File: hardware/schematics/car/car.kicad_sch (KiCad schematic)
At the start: 20 parts, among them M1 Motor_Servo, Q1 PMOS, SW2 SW_Push, SW3 SW_Push, U1 VL53L0CXV0DH1, U10 Mini-560, U11 JGA25-37x, U2 VL53L0CXV0DH1, U3 VL53L0CXV0DH1, U4 Pixy2, U5 TXS0108EPW, U6 TB6612FNG, U7 SparkFun OTOS, U8 SWD debug probe, U9 Mini-360

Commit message: [Schematic] schematic: use TB6612FNG breakout footprint
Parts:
- U6: footprint Package_SO:SSOP-24_5.3x8.2mm_P0.65mm -> xlnc-foot:TB6612FNG_Breakout_Sparkfun
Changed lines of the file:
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@@
 			)
 		)
-		(property "Footprint" "Package_SO:SSOP-24_5.3x8.2mm_P0.65mm"
+		(property "Footprint" "xlnc-foot:TB6612FNG_Breakout_Sparkfun"
 			(at 44.45 186.69 0)
 			(hide yes)

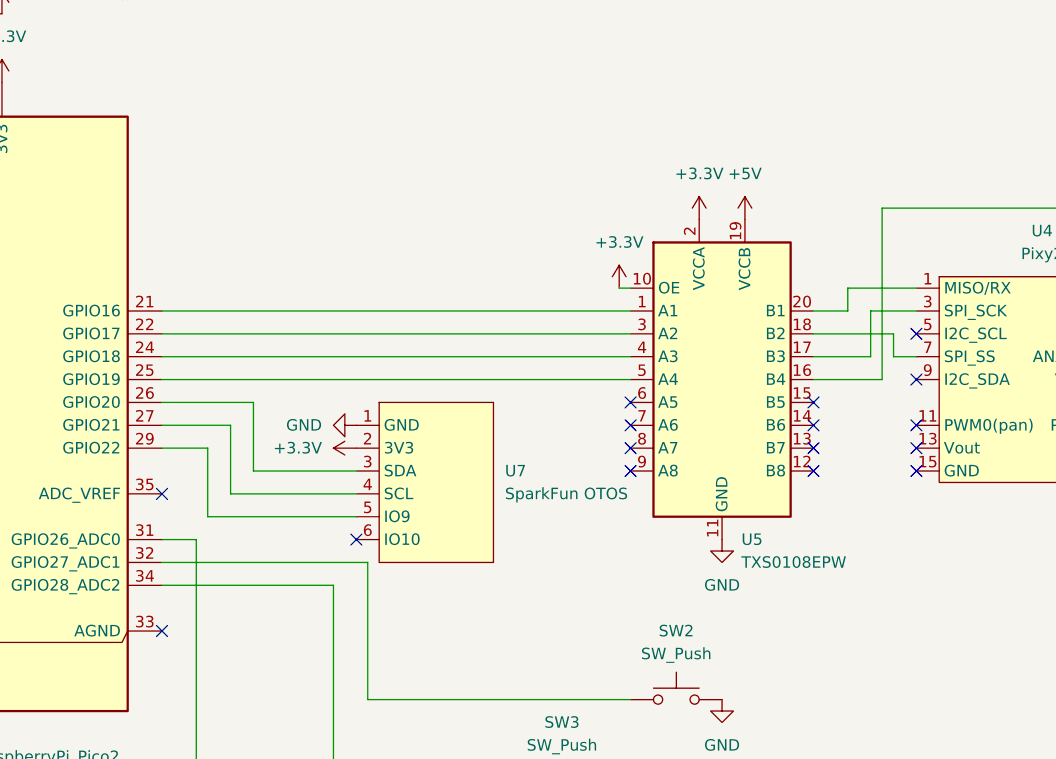
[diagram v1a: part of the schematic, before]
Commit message: [Schematic] Use simpler, smaller level shifter
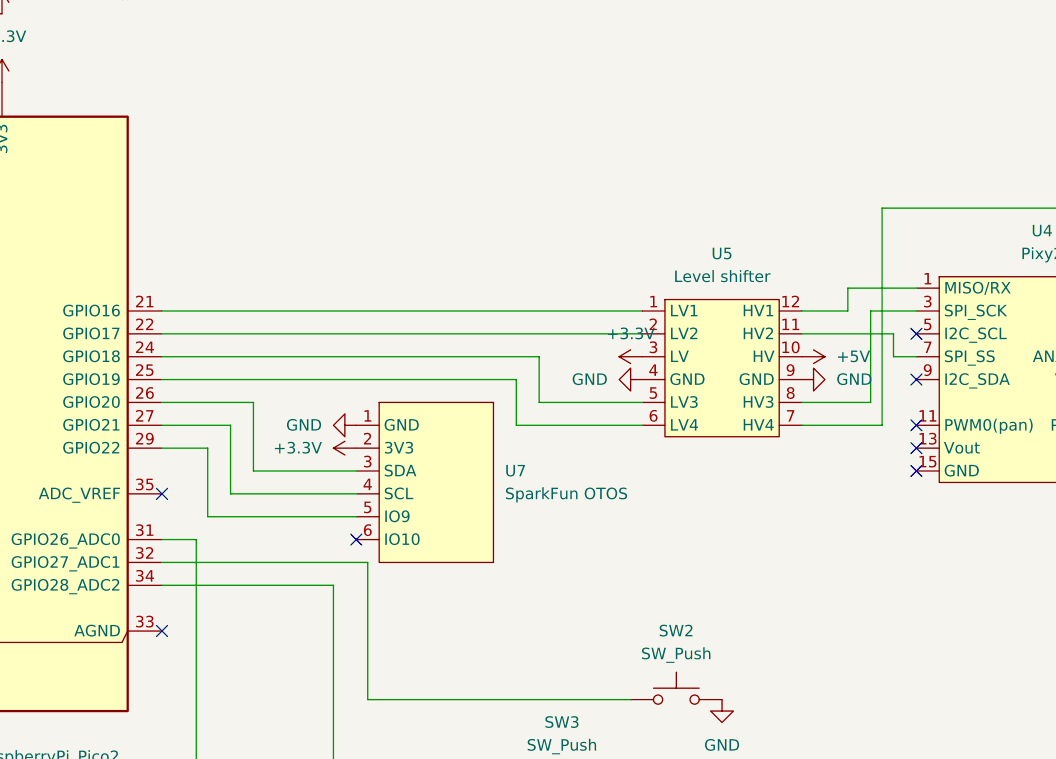
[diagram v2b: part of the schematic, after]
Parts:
- removed U5: TXS0108EPW, Package_SO:TSSOP-20_4.4x6.5mm_P0.65mm, symbol Logic_LevelTranslator:TXS0108EPW
- added U5: Level shifter, xlnc-foot:LevelShifter_4channel_bidirectional, symbol xlnc_apex:LevelShifter_4channel_bidirectional
- BZ1: footprint (none) -> Buzzer_Beeper:Buzzer_TDK_PS1240P02BT_D12.2mm_H6.5mm
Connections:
- net +3.3V: now also U5.3 (LV)
- net +5V: now also U5.10 (HV)
- net GND: now also U5.4 (GND), U5.9 (GND)
- net at A1.21 (GPIO16): now also U5.1 (LV1)
- net at U4.4 (MOSI/TX): now also U5.7 (HV4)
- net at U4.3 (SPI_SCK): now also U5.8 (HV3)
- net at U4.7 (SPI_SS): now also U5.11 (HV2)
- net at U4.1 (MISO/RX): now also U5.12 (HV1)
- net at A1.22 (GPIO17): now also U5.2 (LV2)
- net at A1.24 (GPIO18): now also U5.5 (LV3)
- net at A1.25 (GPIO19): now also U5.6 (LV4)
- no-connect marks 28 -> 20

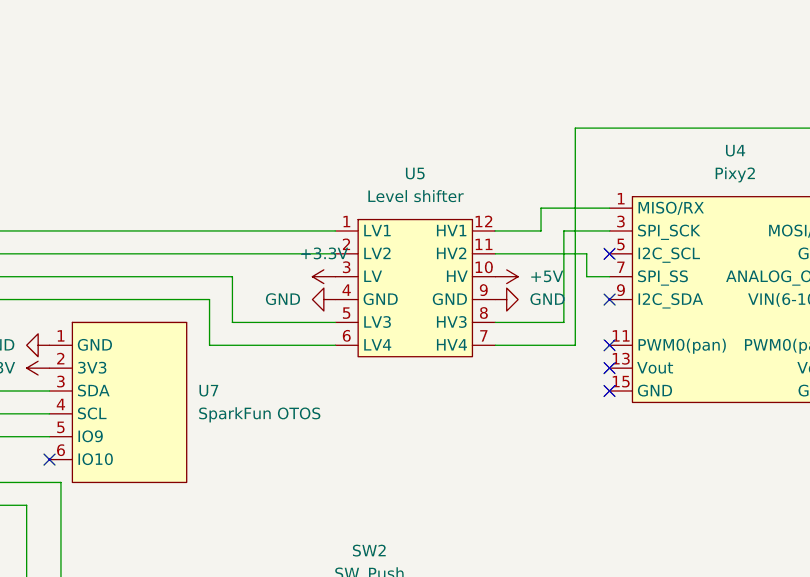
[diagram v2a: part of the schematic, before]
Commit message: [Schematic] Fix super suboptimal connection for level shifter(was like cross thing)
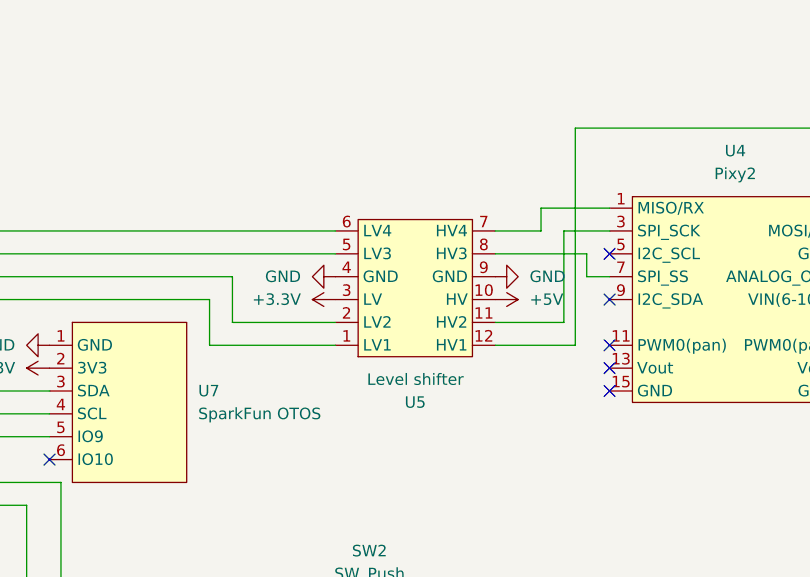
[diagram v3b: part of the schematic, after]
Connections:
- net at U5.1 (LV1): now also A1.25 (GPIO19); no longer A1.21 (GPIO16)
- net at U5.11 (HV2): now also U4.3 (SPI_SCK); no longer U4.7 (SPI_SS)
- net at U5.12 (HV1): now also U4.4 (MOSI/TX); no longer U4.1 (MISO/RX)
- net at U5.2 (LV2): now also A1.24 (GPIO18); no longer A1.22 (GPIO17)
- net at U5.5 (LV3): now also A1.22 (GPIO17); no longer A1.24 (GPIO18)
- net at U5.6 (LV4): now also A1.21 (GPIO16); no longer A1.25 (GPIO19)
- net at U5.7 (HV4): now also U4.1 (MISO/RX); no longer U4.4 (MOSI/TX)
- net at U5.8 (HV3): now also U4.7 (SPI_SS); no longer U4.3 (SPI_SCK)

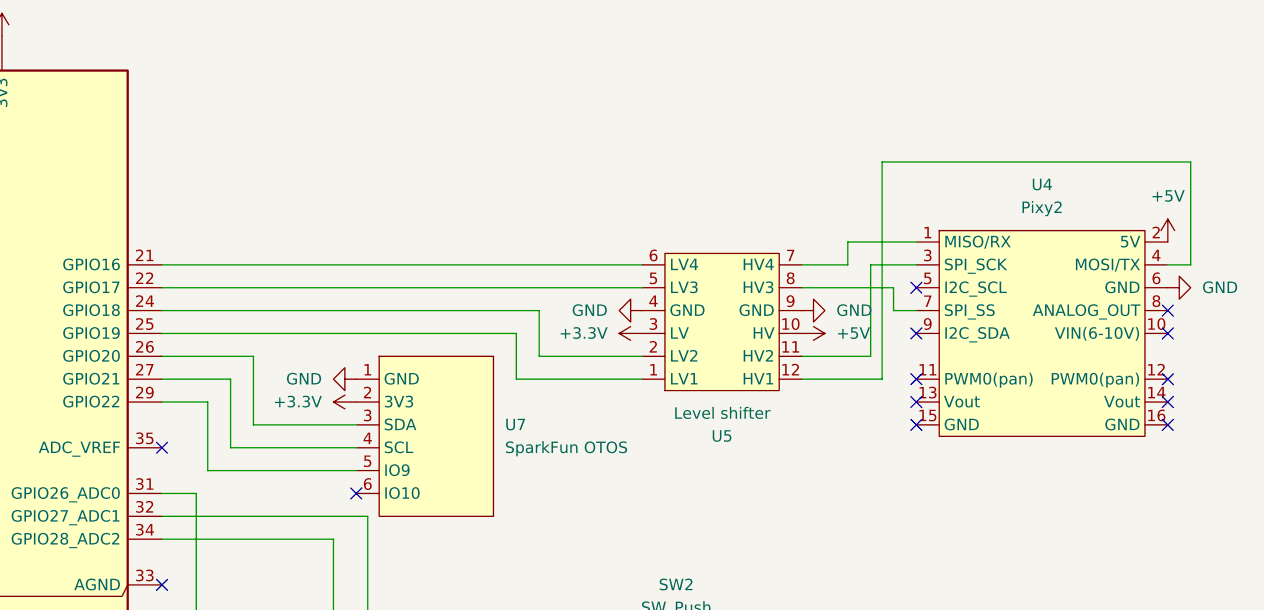
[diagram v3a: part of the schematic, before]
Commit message: [Schematic] Remove level shifter. The pixy2 seems to have 3.3v outputs, maybe 3.3v tolerable input? Need testing.
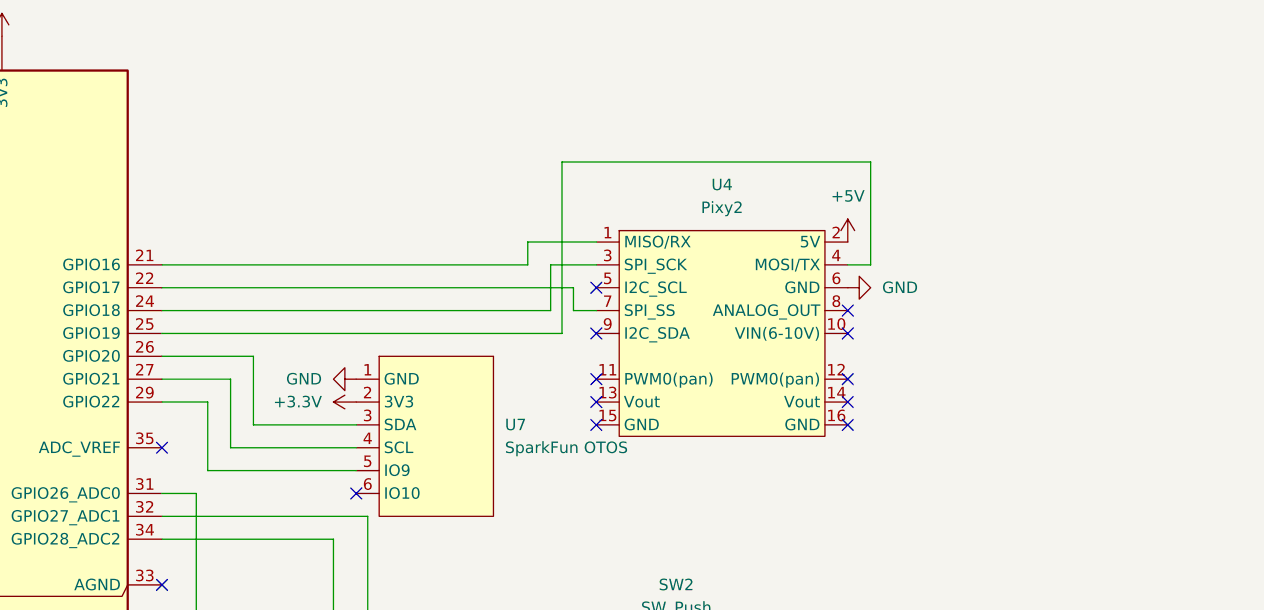
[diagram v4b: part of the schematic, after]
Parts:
- removed U5: Level shifter, xlnc-foot:LevelShifter_4channel_bidirectional, symbol xlnc_apex:LevelShifter_4channel_bidirectional
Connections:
- net at A1.25 (GPIO19): now also U4.4 (MOSI/TX)
- net at U4.3 (SPI_SCK): now also A1.24 (GPIO18)
- net at A1.22 (GPIO17): now also U4.7 (SPI_SS)
- net at A1.21 (GPIO16): now also U4.1 (MISO/RX)
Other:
- moved on the sheet: U4

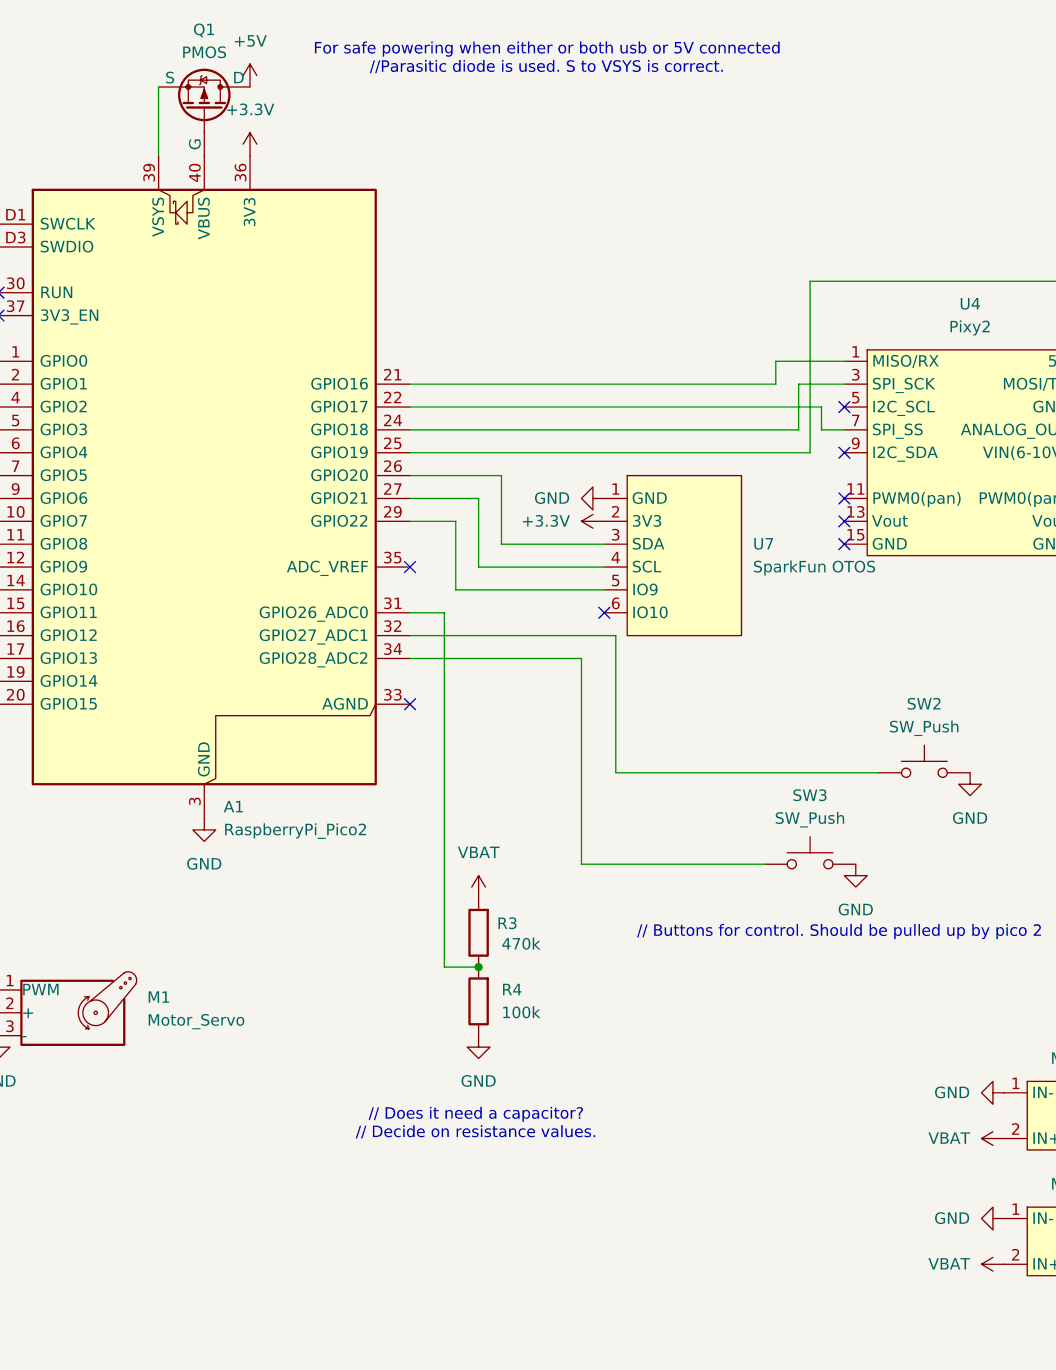
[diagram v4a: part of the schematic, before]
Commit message: [Schematic] fix mosfet, add xt60
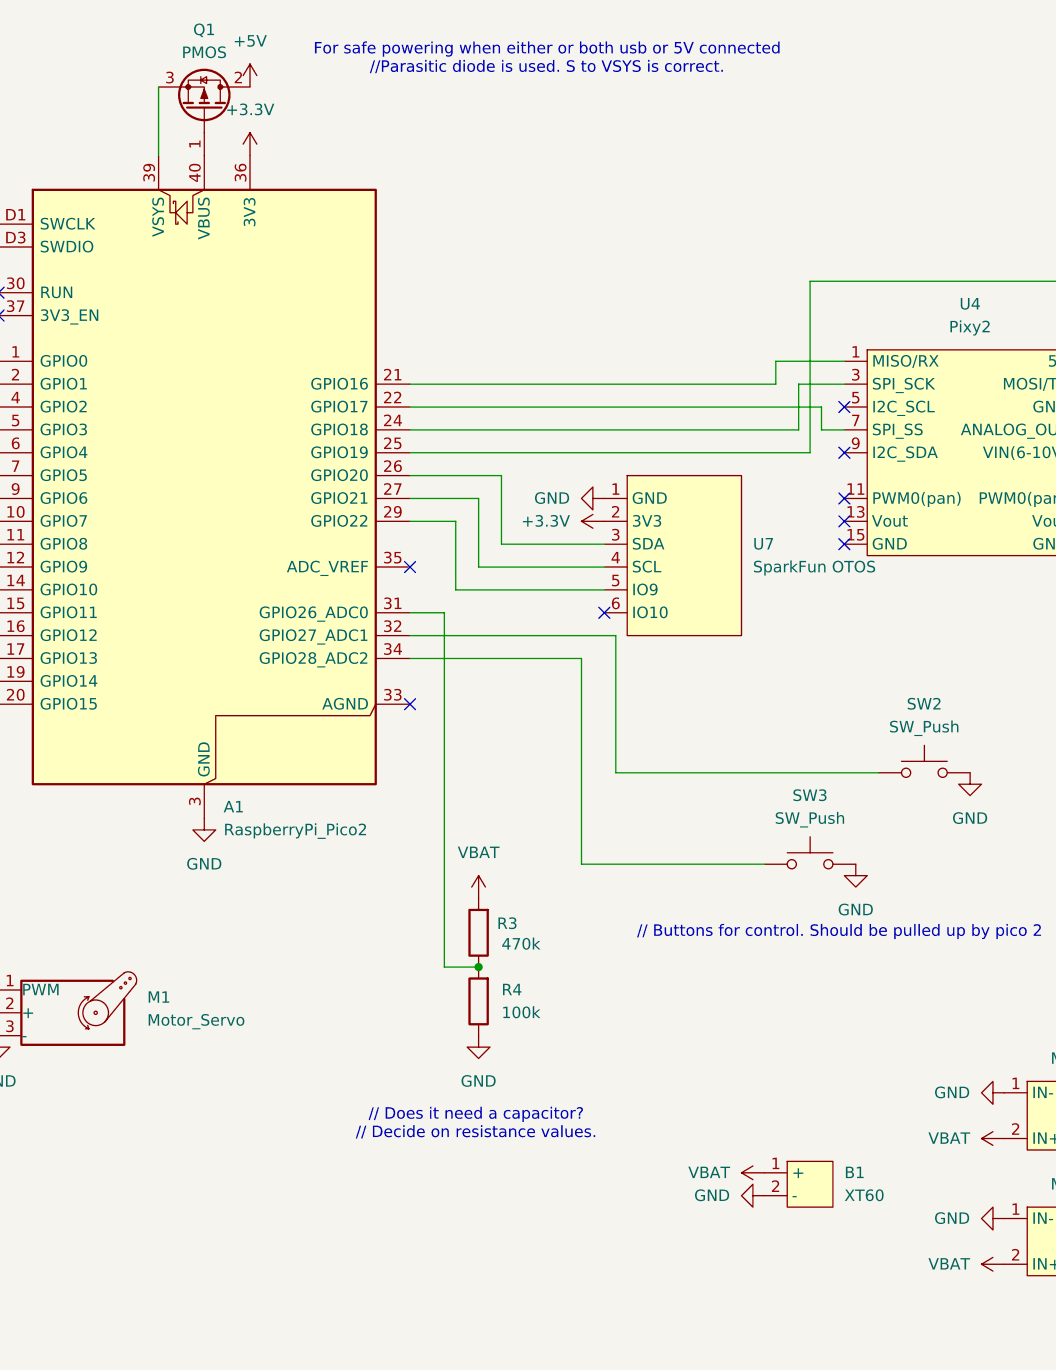
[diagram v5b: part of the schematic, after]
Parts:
- added B1: XT60, xlnc-foot:XT60, symbol xlnc_apex:xt60
- A1: footprint Module:RaspberryPi_Pico_SMD_HandSolder -> Module:RaspberryPi_Pico_Common_THT
- Q1: footprint Package_TO_SOT_THT:TO-247-3_Vertical -> Package_TO_SOT_THT:TO-220F-3_Vertical; symbol Simulation_SPICE:PMOS -> Transistor_FET:Q_PMOS_GDS
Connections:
- net +5V: now also Q1.2 (D); no longer Q1.1 (D)
- net GND: now also B1.2 (-)
- net VBAT: now also B1.1 (+)
- net at A1.40 (VBUS): now also Q1.1 (G); no longer Q1.2 (G)

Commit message: [Schematic] Change button footprint. PCB: move around, connect easy things.
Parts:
- SW2, SW3: footprint Connector_PinHeader_2.54mm:PinHeader_1x02_P2.54mm_Vertical -> xlnc-foot:SW_PUSH_6mm_5.08mm
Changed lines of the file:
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@@
 			)
 		)
-		(property "Footprint" "Connector_PinHeader_2.54mm:PinHeader_1x02_P2.54mm_Vertical"
+		(property "Footprint" "xlnc-foot:SW_PUSH_6mm_5.08mm"
 			(at 208.28 102.87 0)
 			(hide yes)
@@
 			)
 		)
-		(property "Footprint" "Connector_PinHeader_2.54mm:PinHeader_1x02_P2.54mm_Vertical"
+		(property "Footprint" "xlnc-foot:SW_PUSH_6mm_5.08mm"
 			(at 220.98 92.71 0)
 			(hide yes)

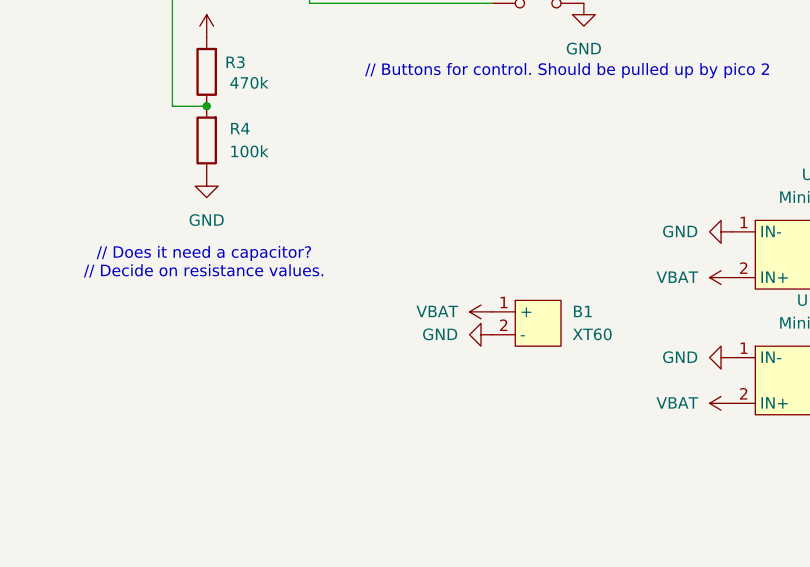
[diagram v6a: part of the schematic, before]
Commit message: [Schematic] Add battery switch.
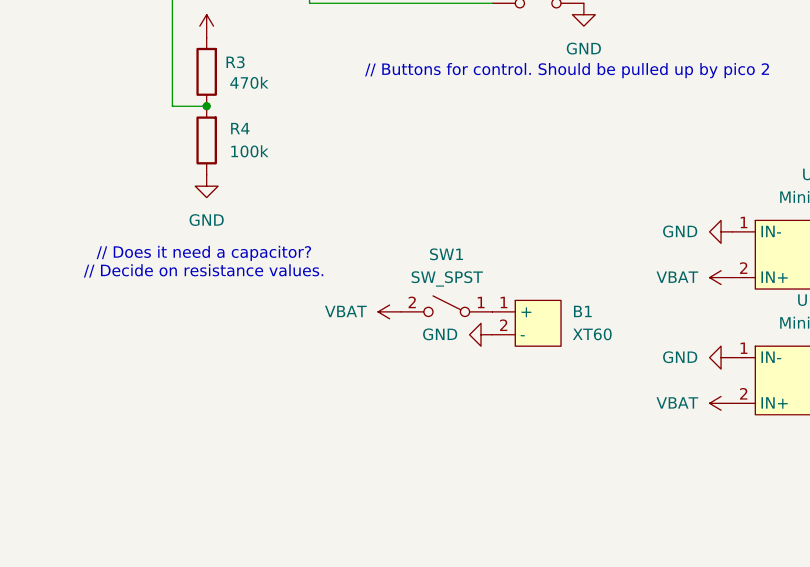
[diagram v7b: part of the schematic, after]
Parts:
- added SW1: SW_SPST, xlnc-foot:SW_SPST_20.96mmx14.74mm, symbol Switch:SW_SPST
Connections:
- net VBAT: now also SW1.2 (B); no longer B1.1 (+)
- new net: B1.1 (+), SW1.1 (A)
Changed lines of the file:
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@@
 	)
 	(symbol
+		(lib_id "Switch:SW_SPST")
+		(at 198.12 142.24 0)
+		(mirror y)
+		(unit 1)
+		(body_style 1)
+		(exclude_from_sim no)
+		(in_bom yes)
+		(on_board yes)
+		(in_pos_files yes)
+		(dnp no)
+		(property "Reference" "SW1"
+			(at 198.12 135.89 0)
+			(show_name no)
+			(do_not_autoplace no)
+			(effects
+				(font
+					(size 1.27 1.27)
+				)
+			)
+		)
+		(property "Value" "SW_SPST"
+			(at 198.12 138.43 0)
+			(show_name no)
+			(do_not_autoplace no)
+			(effects
+				(font
+					(size 1.27 1.27)
+				)
+			)
+		)
+		(property "Footprint" "xlnc-foot:SW_SPST_20.96mmx14.74mm"
+			(at 198.12 142.24 0)
+			(hide yes)
+			(show_name no)
+			(do_not_autoplace no)
+			(effects
+				(font
+					(size 1.27 1.27)
+				)
+			)
+		)
+		(property "Datasheet" ""
+			(at 198.12 142.24 0)
+			(hide yes)
+			(show_name no)
+			(do_not_autoplace no)
+			(effects
+				(font
+					(size 1.27 1.27)
+				)
+			)
+		)
+		(property "Description" "Single Pole Single Throw (SPST) switch"
+			(at 198.12 142.24 0)
+			(hide yes)
+			(show_name no)
+			(do_not_autoplace no)
+			(effects
+				(font
+					(size 1.27 1.27)
+				)
+			)
+		)
+		(pin "1"
+		)
+		(pin "2"
+		)
+		(instances
+			(project "car"
+				(path "/5e1ba60a-5dff-4ce7-a8b0-cf19f27fe16e"
+					(reference "SW1")
+					(unit 1)
+				)
+			)
+		)
+	)
+	(symbol
 		(lib_id "power:GND")
 		(at 247.65 133.35 90)
@@
 	(symbol
 		(lib_id "power:+12V")
-		(at 203.2 142.24 90)
+		(at 193.04 142.24 90)
 		(mirror x)
 		(unit 1)
@@
 		(fields_autoplaced yes)
 		(property "Reference" "#PWR040"
-			(at 207.01 142.24 0)
+			(at 196.85 142.24 0)
 			(hide yes)
 			(show_name no)
@@
 		)
 		(property "Value" "VBAT"
-			(at 199.39 142.2401 90)
+			(at 189.23 142.2401 90)
 			(show_name no)
 			(do_not_autoplace no)
@@
 		)
 		(property "Footprint" ""
-			(at 203.2 142.24 0)
+			(at 193.04 142.24 0)
 			(hide yes)
 			(show_name no)
@@
 		)
 		(property "Datasheet" ""
-			(at 203.2 142.24 0)
+			(at 193.04 142.24 0)
 			(hide yes)
 			(show_name no)
@@
 		)
 		(property "Description" "Power symbol creates a global label with name \"+12V\""
-			(at 203.2 142.24 0)
+			(at 193.04 142.24 0)
 			(hide yes)
 			(show_name no)
